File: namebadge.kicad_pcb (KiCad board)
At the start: 2 copper layers, 73.7 x 132.1 mm, 35 parts, among them IC1 SN74AHCT125N, J1 Barrel_Jack, SW1 SW_Push, U1 Pico

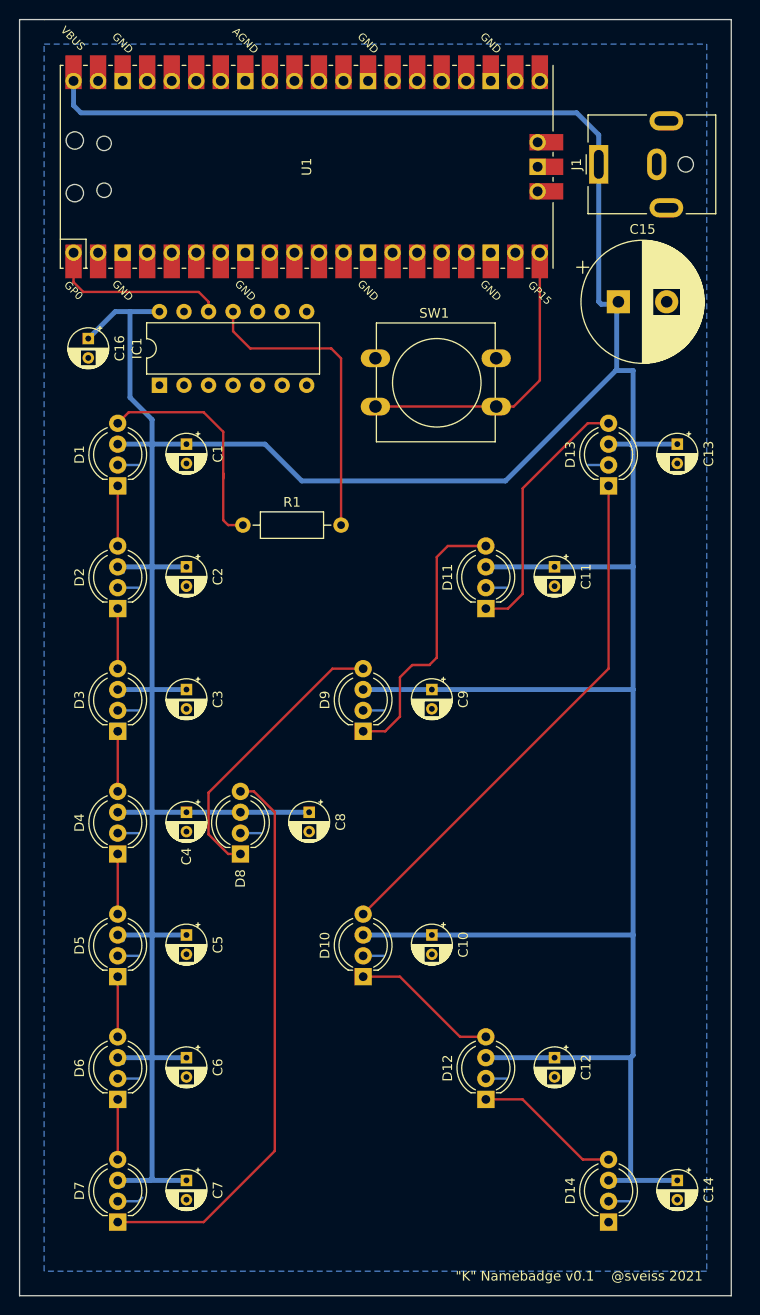
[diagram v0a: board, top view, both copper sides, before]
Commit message: Fix capacitor footprints and Pico location.
Fixes #2, #3.
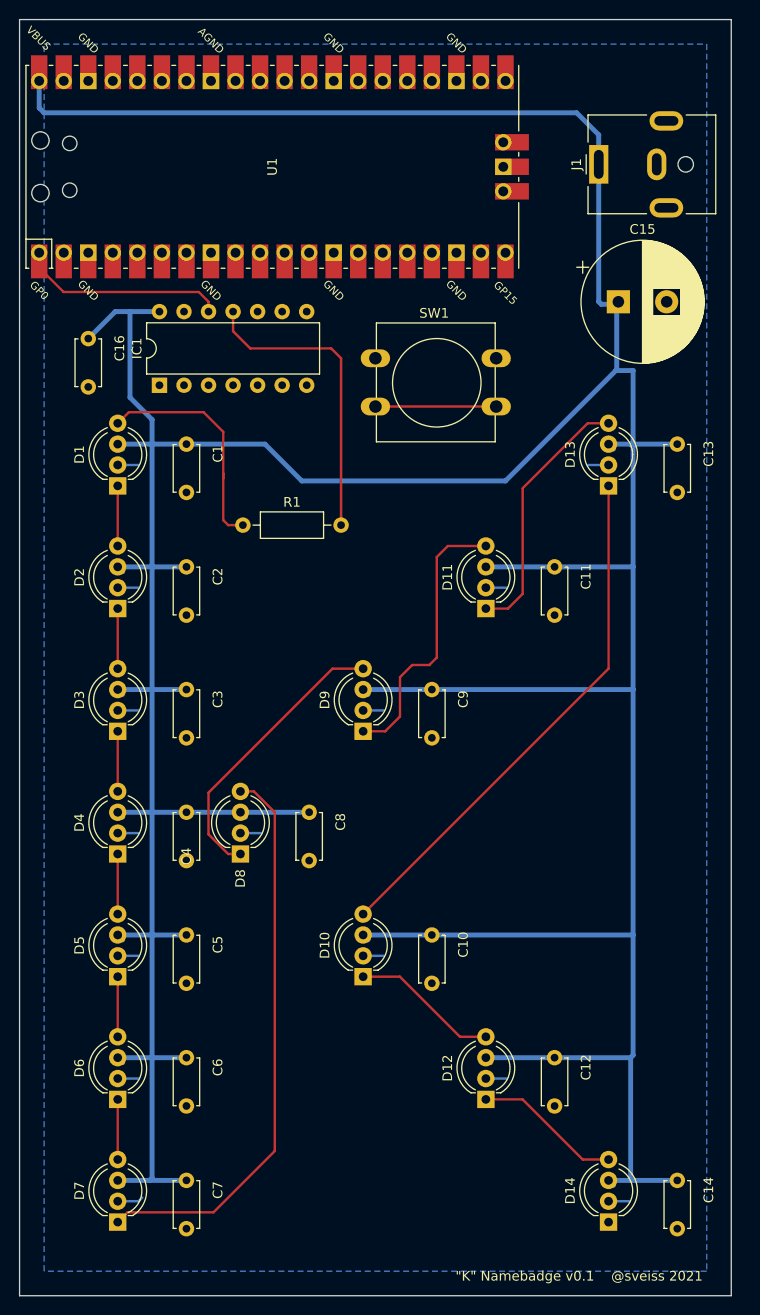
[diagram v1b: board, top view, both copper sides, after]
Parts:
- C1, C10, C11, C12, C13, C14, C16, C2, C3, C4, C5, C6, C7, C8, C9: footprint Capacitor_THT:CP_Radial_D4.0mm_P2.00mm -> Capacitor_THT:C_Disc_D4.7mm_W2.5mm_P5.00mm
- moved U1 3.56 mm to (46.5, 33.0)
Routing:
- net Net-(SW1-Pad2): track 31.4 -> 12.5 mm
- net VCC: track 493.2 -> 496.9 mm
- net Net-(IC1-Pad12): track 18.9 -> 21.6 mm

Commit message: Connect rest of pins on the buffer to VCC/Gnd. Resize copper plane to cover more of the Pico after its move. Fix a couple of unconnected tracks. PCB version on silkscreen to v0.2.
Also updates schematic with capacitor footprint changes.
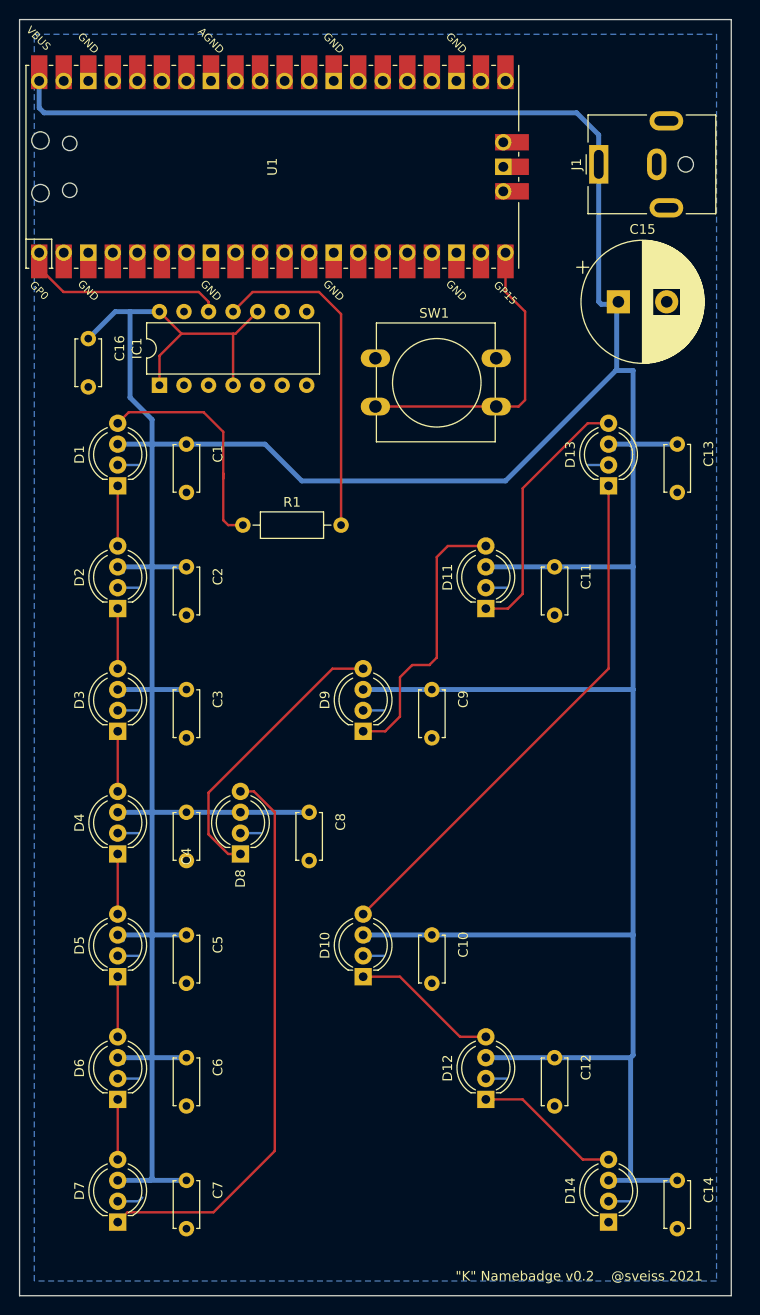
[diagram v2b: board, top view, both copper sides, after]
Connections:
- IC1 pad 1: GND -> VCC
- IC1 pad 10: Net-(IC1-Pad10) -> VCC
- IC1 pad 2: Net-(IC1-Pad2) -> GND
- IC1 pad 3: Net-(IC1-Pad3) -> GND
- IC1 pad 4: Net-(IC1-Pad4) -> VCC
- IC1 pad 5: Net-(IC1-Pad5) -> GND
- IC1 pad 6: Net-(IC1-Pad6) -> GND
- IC1 pad 8: Net-(IC1-Pad8) -> GND
- IC1 pad 9: Net-(IC1-Pad9) -> GND
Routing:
- net VCC: track 496.9 -> 520.6 mm
- net Net-(SW1-Pad2): track 12.5 -> 31.9 mm
- net Net-(IC1-Pad11): track 31.7 -> 34.8 mm
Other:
- board text added: ""K" Namebadge v0.2 @sveiss 2021"
- board text removed: ""K" Namebadge v0.1 @sveiss 2021"

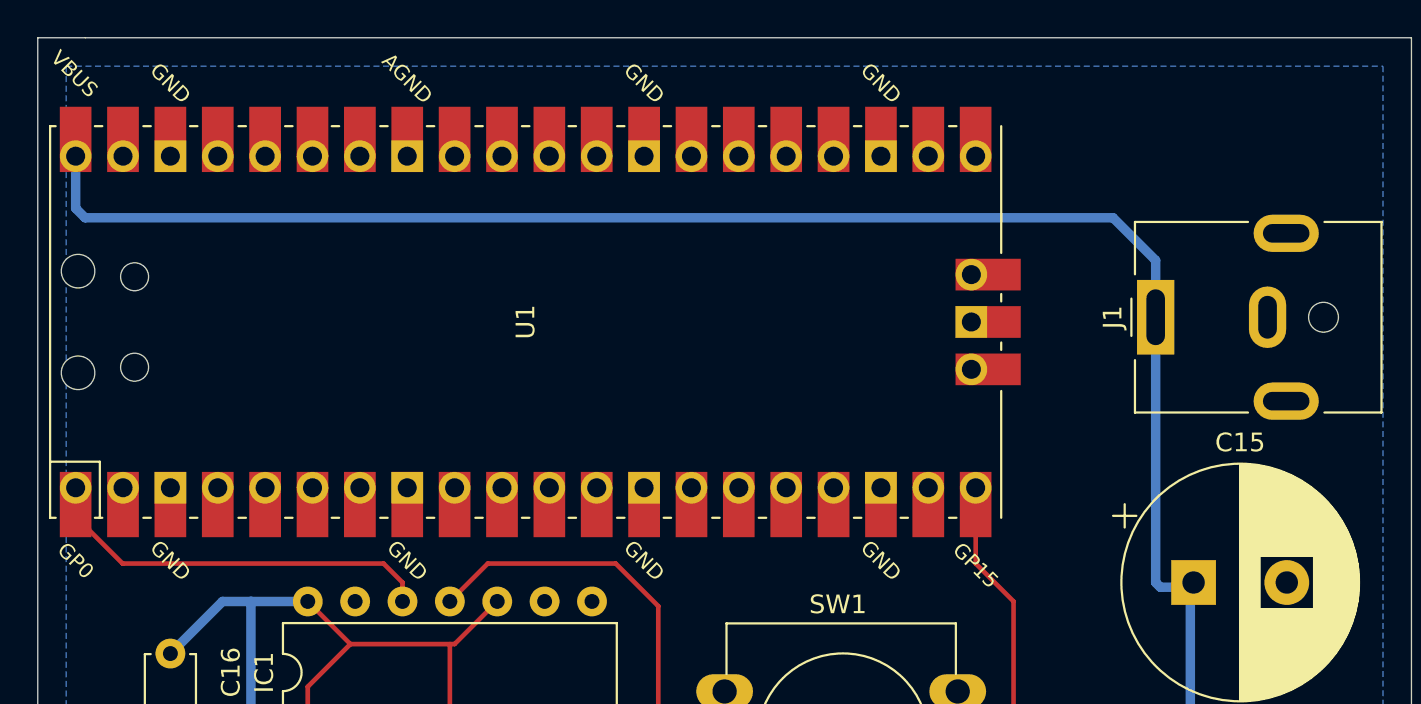
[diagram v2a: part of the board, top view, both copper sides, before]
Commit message: Adds a Schottky on the DC input and moves it to VSYS, not VBUS.
Fixes #4.
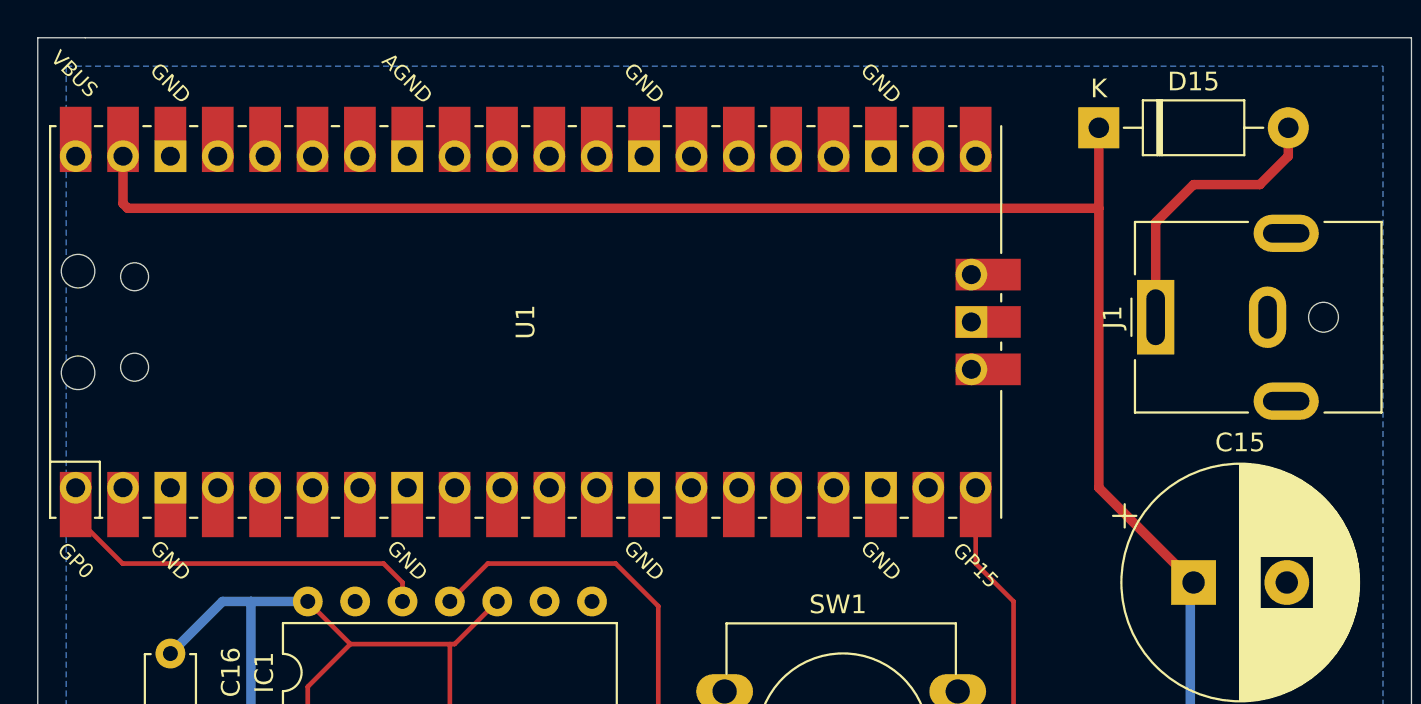
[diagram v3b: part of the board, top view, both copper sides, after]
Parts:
- added D15: D_Schottky, Diode_THT:D_DO-41_SOD81_P10.16mm_Horizontal, F.Cu at (77.2, 22.6)
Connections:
- J1 pad 1: VCC -> Net-(D15-Pad2)
- U1 pad 39: Net-(U1-Pad39) -> VCC
- U1 pad 40: VCC -> Net-(U1-Pad40)
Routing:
- net Net-(D15-Pad2): track 0.00 -> 16.0 mm
